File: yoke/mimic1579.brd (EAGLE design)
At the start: 165.1 x 114.3 mm, 77 parts, among them J1 44PINEDGE, P1 2K, P2 2K, Q1 2N3904, Q10 2N3906, Q11 2N3904, Q12 2N3906, Q13 2N3904, Q2 2N3904, Q3 2N3904, Q4 2N3906, Q5 2N3904, Q6 2N3906, Q7 2N3904, Q8 2N3906, Q9 2N3904

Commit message: revised artwork
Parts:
- P3: value 44PINEDGE -> 44PINEDGE-M
- R29, R34: value 475 -> 1.5K
- R30, R33, R35: value 1.5K -> 475
- R31: value 4.75K -> 1.5K
- R32: value 475 -> 4.75K
- moved R31 117.0 mm to (145.3, 29.8)
- moved R33 101.8 mm to (43.7, 23.2), turned to 180 degrees
- moved R34 101.8 mm to (145.3, 23.1)
- moved R35 101.8 mm to (43.7, 16.5)
- moved R29 101.8 mm to (145.3, 36.6)
- moved R30 101.8 mm to (43.7, 30.1)
- moved D5 35.9 mm to (127.5, 70.7)
- moved D6 35.9 mm to (91.9, 66.0)
- moved D11 18.0 mm to (109.7, 50.4)
- moved D12 18.0 mm to (91.9, 47.9)
- moved R32 15.2 mm to (28.4, 23.2), turned to 0 degrees
- renumbered J1 to P3
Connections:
- net -15V: now also R29.2, R31.2, R34.2; no longer R30.2, R33.2, R35.2
- net GND: now also P3.4
- net N$11: now also R31.1, R34.1; no longer R33.1, R35.1
- net N$13: now also R30.1; no longer R29.1
- net N$14: now also R35.1; no longer R34.1
- net N$15: now also R33.2; no longer R31.2
- net N$18: now also D5.C; no longer D6.C
- net N$21: now also R29.1; no longer R30.1
- net N$23: now also R30.2; no longer R29.2
- net N$25: now also R33.1, R35.2; no longer R32.1, R34.2
- net N$5: now also D11.A; no longer D12.A
- net N$6: now also D6.C; no longer D5.C
- net U_IN: now also R32.1; no longer R31.1
- net VREF1: now also D12.A; no longer D11.A
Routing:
- net GND: track 158.0 -> 167.1 mm, vias 2 -> 4
- net H_OUT: track 72.6 -> 67.4 mm
- net P_OUT: track 147.8 -> 143.3 mm
- net N$5: track 133.3 -> 132.0 mm
- net L_IN: track 43.7 -> 42.4 mm
- net U_IN: track 30.4 -> 31.4 mm

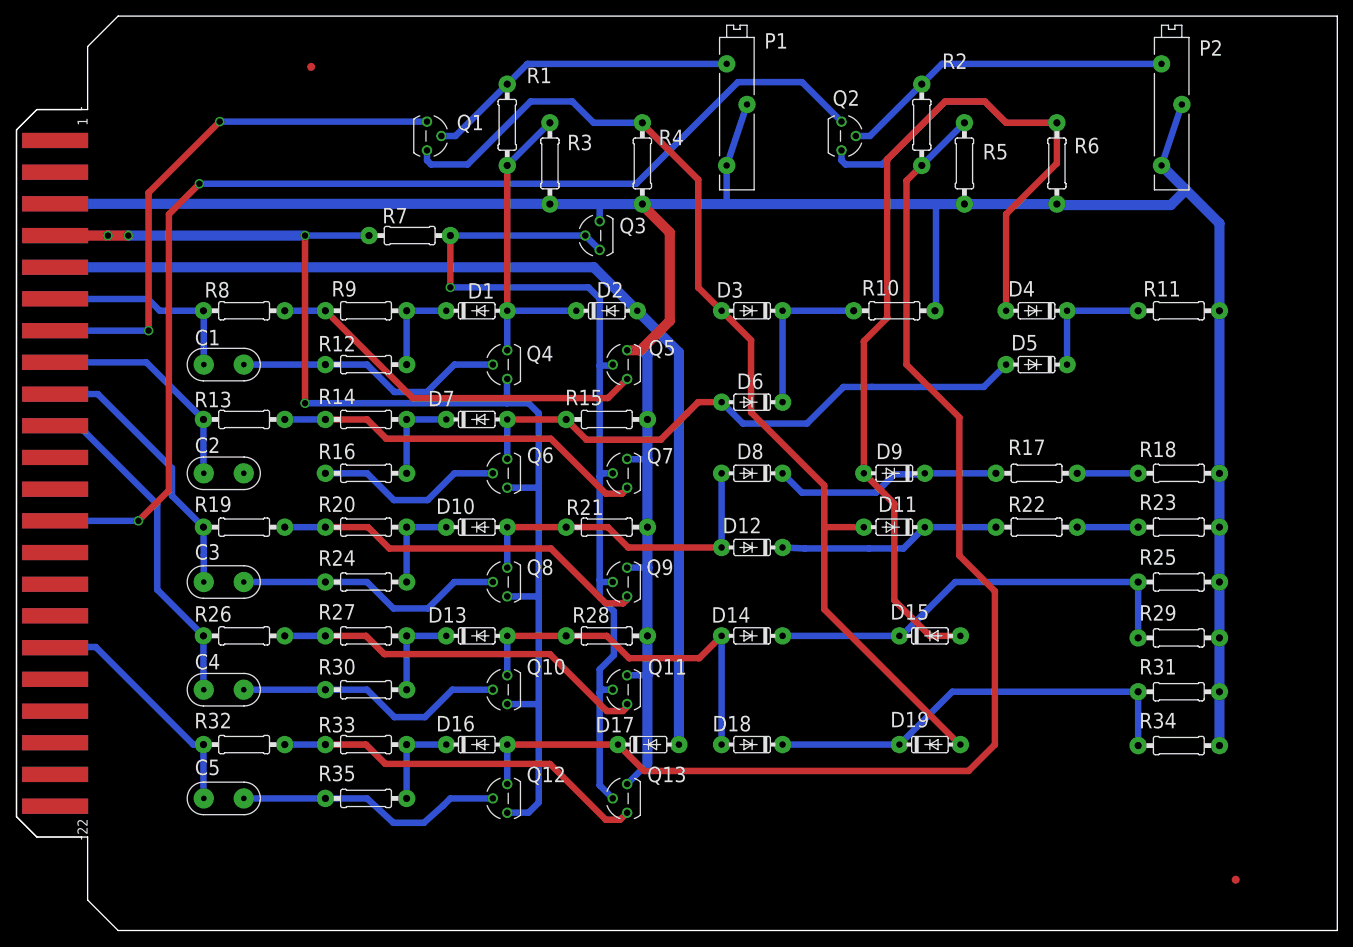
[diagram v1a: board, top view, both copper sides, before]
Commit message: added missing connector on bckplane
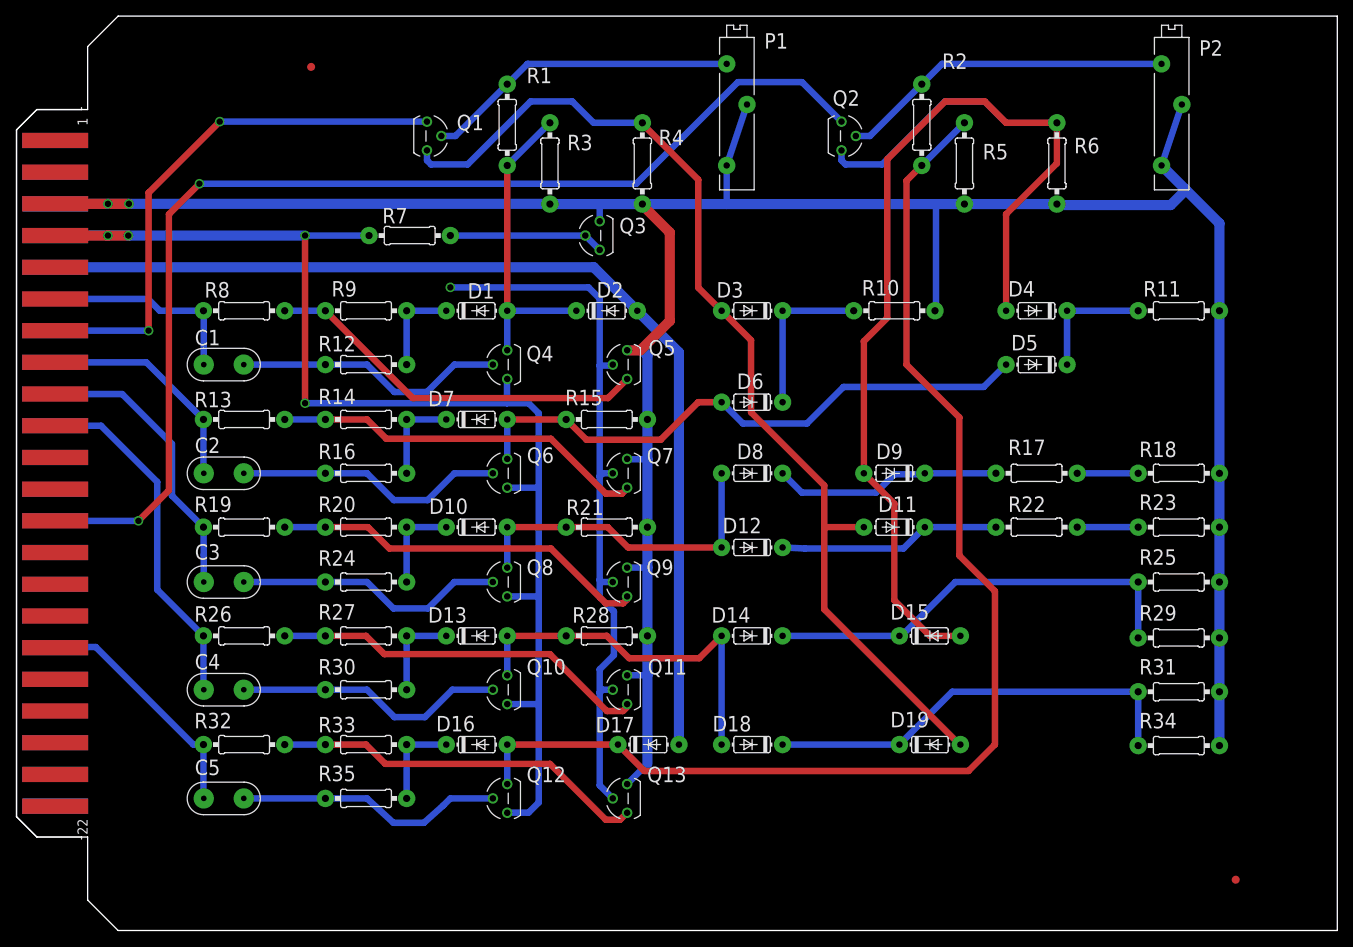
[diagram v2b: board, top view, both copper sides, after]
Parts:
- D1, D10, D11, D12, D13, D14, D15, D16, D17, D18, D19, D2, D3, D4, D5, D6, D7, D8, D9: device keiths:DO35-7 -> replacements:DO35-7
- R1, R10, R11, R12, R13, R14, R15, R16, R17, R18, R19, R2, R20, R21, R22, R23, R24, R25, R26, R27, R28, R29, R3, R30, R31, R32, R33, R34, R35, R4, R5, R6, R7, R8, R9: device keiths:0207/10 -> replacements:0207/10
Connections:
- new net N$24: Q3.2, Q3.3, R7.1
- net -15V: now also P3.3
- net N$33: no longer Q3.2, Q3.3, R7.1
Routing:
- net N$33: track 116.8 -> 91.3 mm
- net N$24: track 0.00 -> 19.4 mm
- net -15V: track 342.2 -> 361.1 mm, vias 0 -> 2
- net N$30: track 23.7 -> 33.9 mm
- net K_IN: track 34.3 -> 36.1 mm
- net L_IN: track 42.4 -> 44.1 mm
